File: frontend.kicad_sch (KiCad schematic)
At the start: 76 parts, among them J10 GND_CLIP, J3 RF-SHIELD-FRAME, J4 MOUNTING_HOLE, J5 MOUNTING_HOLE, J6 MOUNTING_HOLE, J7 MOUNTING_HOLE, P4 SMA, Q1 NMOS/PMOS, Q14 Q_PMOS_GSD, Q8 BFR840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

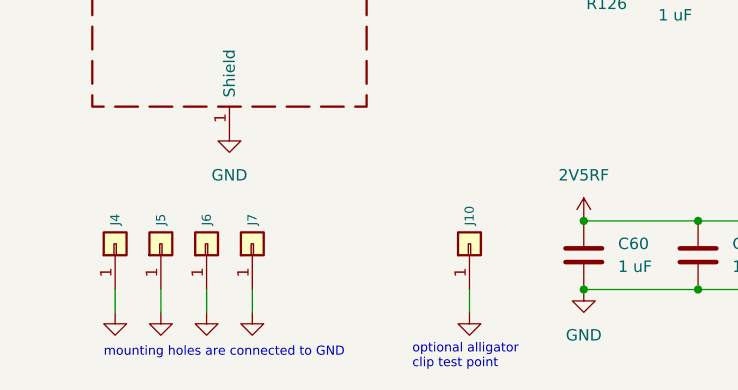
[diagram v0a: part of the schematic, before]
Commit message: Update symbols and footprints
- Update U21 symbol and footprint
- Add L10, L11 3D model
- Add T1, T2 3D model
- Update U29 footprint
- Update J10 footprint and part selection, change to TP6
- Update diode footprints and 3D models
- Update SMA connector footprint
- Fix 3D model scale for various footprints
- Change L1 from 0603 back to 0201
- Fix pin header 3D models
- Add component substitutions
- Update RF switch and amplifier footprints
- Remove fiducials
- Update mounting hole symbol and footprint
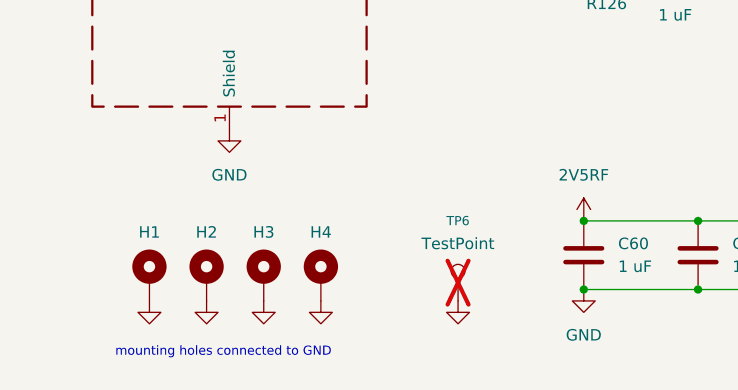
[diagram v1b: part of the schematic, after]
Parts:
- removed J4, J5, J6, J7: MOUNTING_HOLE, hackrf:GSG-HOLE126MIL-COPPER, symbol Connector_Generic:Conn_01x01
- added H1, H2, H3, H4: MountingHole_Pad, praline:MountingHole_3.2mm_M3_Pad_Via, symbol Mechanical:MountingHole_Pad
- P4: Substitution (none) -> M04-0102170R0A
- TP6: renamed from J10; value GND_CLIP -> TestPoint; footprint hackrf:GSG-TEST-POINT-S1751-46R -> TestPoint:TestPoint_Loop_D1.80mm_Drill1.0mm_Beaded; symbol Connector_Generic:Conn_01x01 -> Connector:TestPoint; Manufacturer Harwin -> Ronghe; Part Number S1751-46R -> RH-5001; now not fitted
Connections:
- net GND: now also H1.1, H2.1, H3.1, H4.1
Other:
- note added: "mounting holes connected to GND"
- note removed: "mounting holes are connected to GND"
- note removed: "optional alligator clip test point"

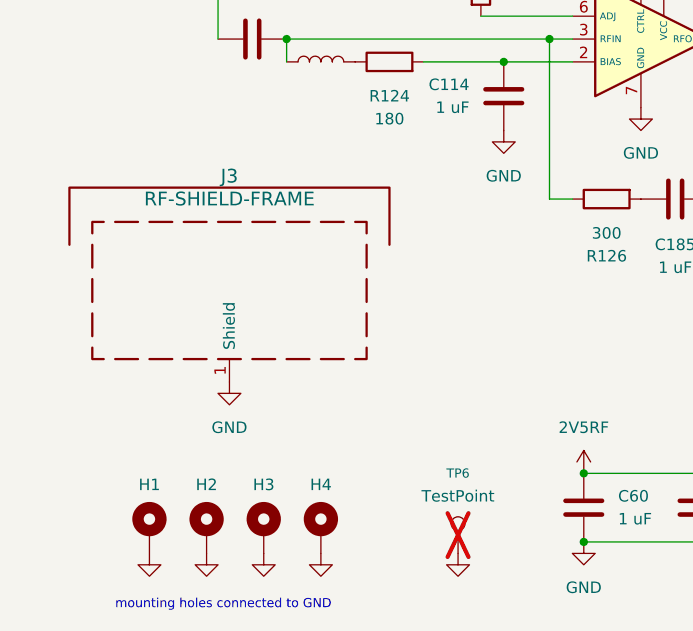
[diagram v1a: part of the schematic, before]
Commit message: Add M2 mounting holes
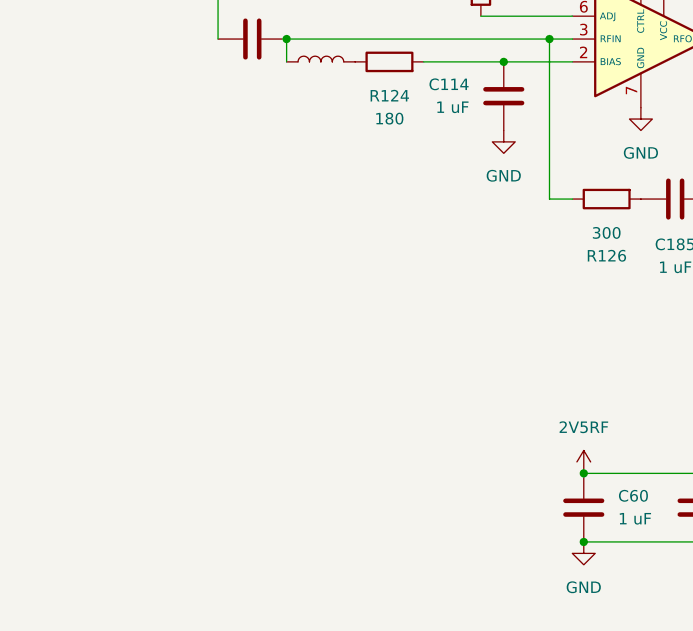
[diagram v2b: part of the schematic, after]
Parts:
- removed H1, H2, H3, H4: MountingHole_Pad, praline:MountingHole_3.2mm_M3_Pad_Via, symbol Mechanical:MountingHole_Pad
- removed J3: RF-SHIELD-FRAME, praline:Laird_Technologies_BMI-S-230-F_50.8x38.1mm, symbol Device:RFShield_TwoPieces
- removed TP6: TestPoint, TestPoint:TestPoint_Loop_D1.80mm_Drill1.0mm_Beaded, symbol Connector:TestPoint
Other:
- note removed: "mounting holes connected to GND"

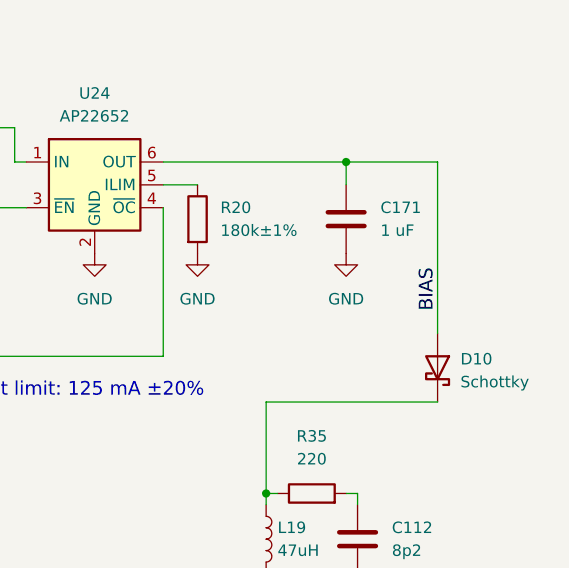
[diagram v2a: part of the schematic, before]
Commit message: Add test points
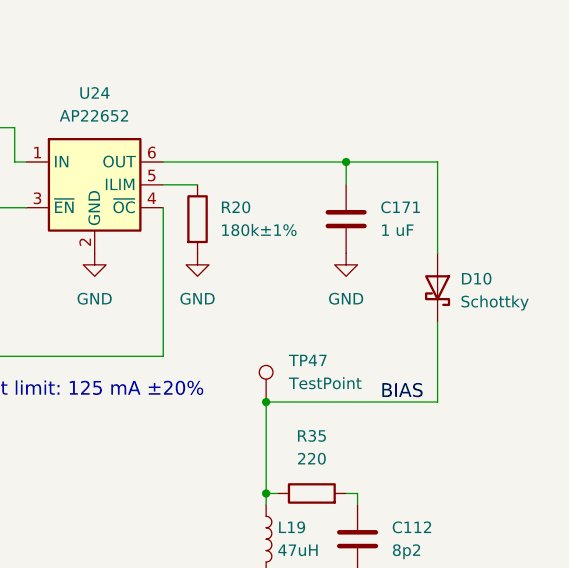
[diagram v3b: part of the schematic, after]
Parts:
- added TP47: TestPoint, TestPoint:TestPoint_Pad_D1.0mm, symbol Connector:TestPoint
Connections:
- net BIAS: now also D10.1 (K), L19.1, R35.1, TP47.1; no longer C171.1, D10.2 (A), U24.6 (OUT)
- new net: C171.1, D10.2 (A), U24.6 (OUT)
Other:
- moved on the sheet: D10
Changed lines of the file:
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@@
 	)
 	(junction
+		(at 241.3 64.77)
+		(diameter 0)
+		(color 0 0 0 0)
+	)
+	(junction
 		(at 143.51 63.5)
 		(diameter 0)
@@
 	(wire
 		(pts
+			(xy 241.3 64.77) (xy 260.35 64.77)
+		)
+		(stroke
+			(width 0)
+			(type default)
+		)
+	)
+	(wire
+		(pts
 			(xy 143.51 38.1) (xy 143.51 45.72)
 		)
@@
 	(wire
 		(pts
+			(xy 260.35 55.88) (xy 260.35 64.77)
+		)
+		(stroke
+			(width 0)
+			(type default)
+		)
+	)
+	(wire
+		(pts
 			(xy 191.77 132.08) (xy 193.04 132.08)
 		)
@@
 	(wire
 		(pts
-			(xy 260.35 57.15) (xy 260.35 38.1)
+			(xy 260.35 48.26) (xy 260.35 38.1)
 		)
 		(stroke
@@
 	(wire
 		(pts
-			(xy 260.35 64.77) (xy 241.3 64.77)
-		)
-		(stroke
-			(width 0)
-			(type default)
-		)
-	)
-	(wire
-		(pts
 			(xy 143.51 53.34) (xy 171.45 53.34)
 		)
@@
 	)
 	(label "BIAS"
-		(at 260.35 54.61 90)
+		(at 254 64.77 0)
 		(effects
 			(font
@@
 	(symbol
 		(lib_id "Device:D_Schottky")
-		(at 260.35 60.96 270)
+		(at 260.35 52.07 270)
 		(mirror x)
 		(unit 1)
@@
 		(fields_autoplaced yes)
 		(property "Reference" "D10"
-			(at 262.89 60.0074 90)
+			(at 262.89 51.1174 90)
 			(effects
 				(font
@@
 		)
 		(property "Value" "Schottky"
-			(at 262.89 62.5474 90)
+			(at 262.89 53.6574 90)
 			(effects
 				(font
@@
 		)
 		(property "Footprint" "praline:TSLP-2-19"
-			(at 260.35 60.96 0)
+			(at 260.35 52.07 0)
 			(effects
 				(font
@@
 		)
 		(property "Datasheet" "~"
-			(at 260.35 60.96 0)
+			(at 260.35 52.07 0)
 			(effects
 				(font
@@
 		)
 		(property "Description" "DIODE SCHOTTKY 40V 1A DSN1006-2"
-			(at 260.35 60.96 0)
+			(at 260.35 52.07 0)
 			(effects
 				(font
@@
 		)
 		(property "Manufacturer" "Nexperia"
-			(at 260.35 60.96 0)
+			(at 260.35 52.07 0)
 			(effects
 				(font
@@
 		)
 		(property "Part Number" "PMEG4010ESBYL"
-			(at 260.35 60.96 0)
+			(at 260.35 52.07 0)
 			(effects
 				(font
@@
 					(unit 1)
 				)
+			)
+		)
+	)
+	(symbol
+		(lib_id "Connector:TestPoint")
+		(at 241.3 64.77 0)
+		(unit 1)
+		(exclude_from_sim no)
+		(in_bom no)
+		(on_board yes)
+		(dnp no)
+		(fields_autoplaced yes)
+		(property "Reference" "TP47"
+			(at 243.84 60.1979 0)
+			(effects
+				(font
+					(size 1.27 1.27)
+				)
+				(justify left)
+			)
+		)
+		(property "Value" "TestPoint"
+			(at 243.84 62.7379 0)
+			(effects
+				(font
+					(size 1.27 1.27)
+				)
+				(justify left)
+			)
+		)
+		(property "Footprint" "TestPoint:TestPoint_Pad_D1.0mm"
+			(at 246.38 64.77 0)
+			(effects
+				(font
+					(size 1.27 1.27)
+				)
+				(hide yes)
+			)
+		)
+		(property "Datasheet" "~"
+			(at 246.38 64.77 0)
+			(effects
+				(font
+					(size 1.27 1.27)
+				)
+				(hide yes)
+			)
+		)
+		(property "Description" ""
+			(at 241.3 64.77 0)
+			(effects
+				(font
+					(size 1.27 1.27)
+				)
+				(hide yes)
+			)
+		)
+		(pin "1"
+		)
+		(instances
+			(project "praline"
+				(path "/dba4afc6-760f-46cb-a936-032b76448f03/00000000-0000-0000-0000-0000503bb638"
+					(reference "TP47")
+					(unit 1)
+				)

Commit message: Use consistent footprints for 0402 and 0201 diodes
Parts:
- D1: footprint Diode_SMD:Nexperia_DSN0603-2_0.6x0.3mm_P0.4mm -> praline:TSSLP-2-1
- Q14: Manufacturer NRC -> LRC
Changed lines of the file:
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@@
 			)
 		)
-		(property "Manufacturer" "NRC"
+		(property "Manufacturer" "LRC"
 			(at 148.59 33.02 0)
 			(effects
@@
 			)
 		)
-		(property "Footprint" "Diode_SMD:Nexperia_DSN0603-2_0.6x0.3mm_P0.4mm"
+		(property "Footprint" "praline:TSSLP-2-1"
 			(at 246.38 105.41 0)
 			(effects

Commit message: Correct component metadata
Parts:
- R43: Part Number RC0402JR-073RL -> RC0201JR-073RL
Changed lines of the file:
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@@
 			)
 		)
-		(property "Description" "RES 3 OHM 5% 1/16W 0402"
+		(property "Description" "RES 3 OHM 5% 1/20W 0201"
 			(at 113.03 129.54 0)
 			(effects
@@
 			)
 		)
-		(property "Part Number" "RC0402JR-073RL"
+		(property "Part Number" "RC0201JR-073RL"
 			(at 113.03 129.54 90)
 			(effects
@@
 					(size 1.27 1.27)
 				)
-				(hide yes)
 			)
 		)
@@
 					(size 1.27 1.27)
 				)
-				(hide yes)
-			)
-		)
+			)
+		)

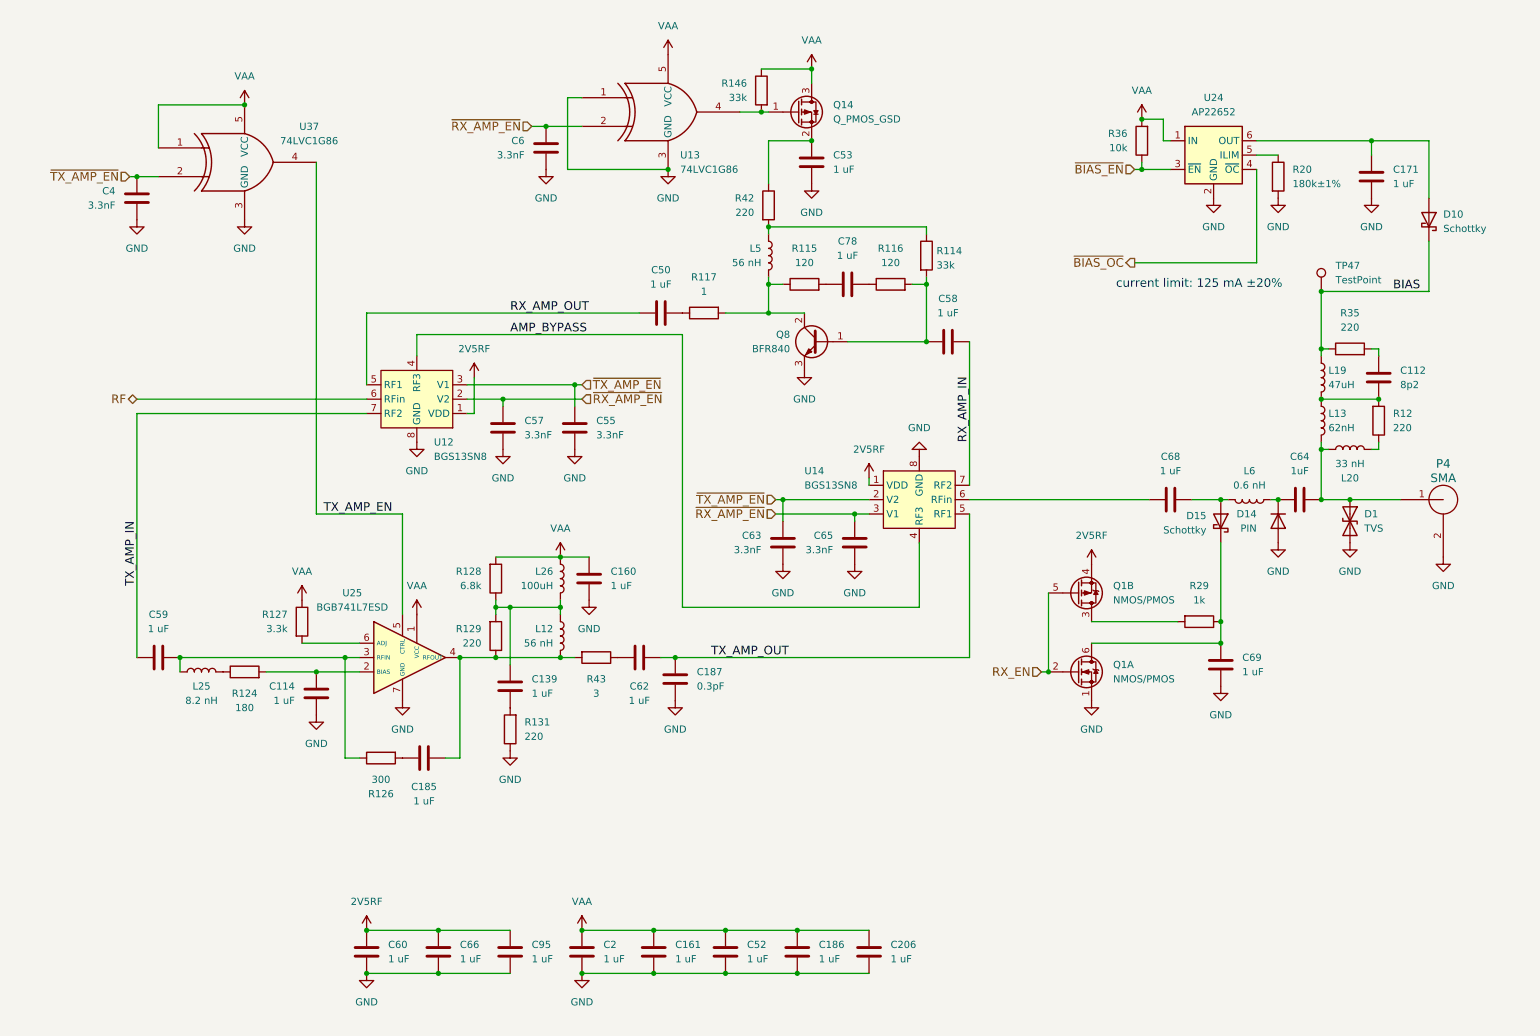
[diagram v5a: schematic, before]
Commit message: Change RX RF amplifier to BGB741
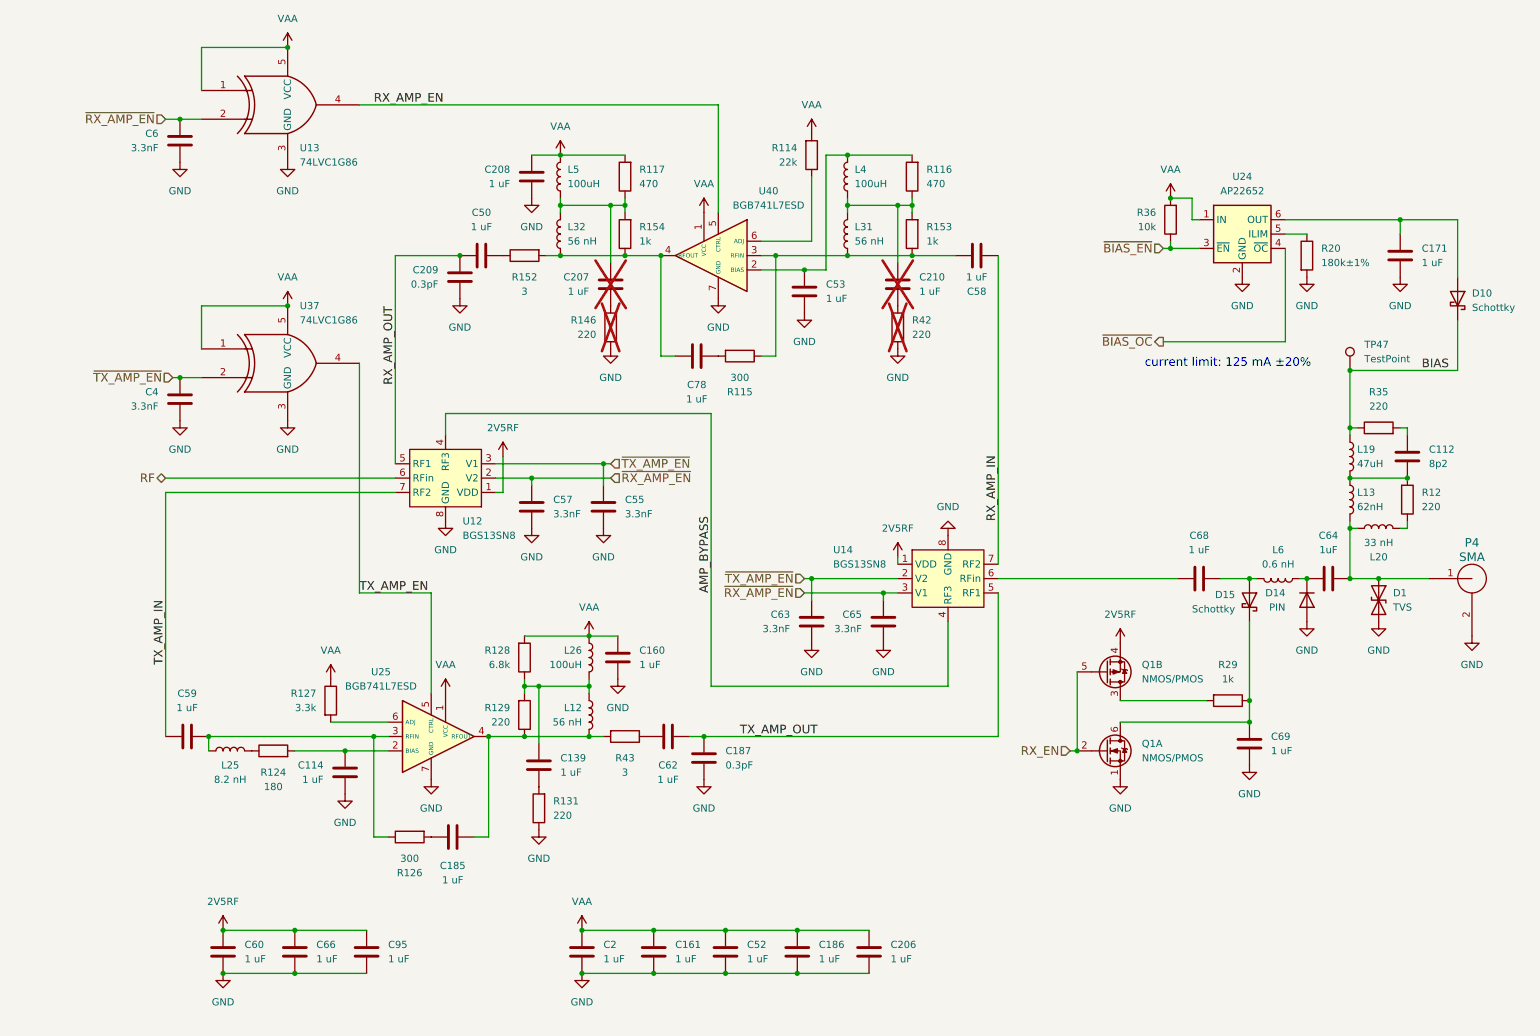
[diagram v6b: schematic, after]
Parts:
- removed Q14: Q_PMOS_GSD, praline:TSLP-3-9, symbol Transistor_FET:Q_PMOS_GSD
- removed Q8: BFR840, praline:TSLP-3-9, symbol Transistor_BJT:Q_NPN_BCE
- added C207, C208, C210: 1 uF, Capacitor_SMD:C_0201_0603Metric, symbol Device:C
- added C209: 0.3pF, Capacitor_SMD:C_0201_0603Metric, symbol Device:C
- added L31, L32: 56 nH, Inductor_SMD:L_0201_0603Metric, symbol Device:L
- added L4: 100uH, praline:L_TDK_MLZ2012_h1.25mm, symbol Device:L
- added R152: 3, Resistor_SMD:R_0201_0603Metric, symbol Device:R
- added R153, R154: 1k, Resistor_SMD:R_0201_0603Metric, symbol Device:R
- added U40: BGB741L7ESD, praline:TSLP-7-1, symbol praline:BGB741L7ESD
- L5: value 56 nH -> 100uH; footprint Inductor_SMD:L_0201_0603Metric -> praline:L_TDK_MLZ2012_h1.25mm; Manufacturer Murata -> TDK; Part Number LQP03TN56NJ02D -> MLZ2012N101LT000; Substitution LQP03TN56NH02D -> MLZ2012N101LTD25
- R114: value 33k -> 22k; Part Number RC0201JR-0733KL -> RC0201FR-0722K6L
- R115: value 120 -> 300; Part Number RC0201FR-07120RL -> RC0201FR-07300RL
- R116: value 120 -> 470; Part Number RC0201FR-07120RL -> RC0201JR-07470RL
- R117: value 1 -> 470; Part Number RC0201JR-071RL -> RC0201JR-07470RL
- R146: value 33k -> 220; Part Number RC0201JR-0733KL -> RC0201JR-07220RL; now not fitted
- R42: now not fitted
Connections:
- net GND: now also R146.1, R42.1, C208.2, C209.2, U40.7 (GND); no longer U13.1
- net RX_AMP_OUT: now also C209.1
- net VAA: now also L5.1, R114.2, R117.2, U13.1, C208.1, U40.1 (VCC); no longer R146.1
- net at C53.1: now also R116.2, L4.1, U40.2 (BIAS); no longer R42.1
- net at C50.2: now also R152.1; no longer R117.1
- net at R146.2: now also C207.2; no longer U13.4
- net at C78.1: now also L32.2, R152.2, R154.1, U40.4 (RFOUT); no longer R115.2
- net at R116.1: now also C210.1, L31.1, L4.2, R153.2; no longer C78.2
- new net: C58.2, L31.2, R115.1, R153.1, U40.3 (RFIN)
- new net: C78.2, R115.2
- new net: R114.1, U40.6 (ADJ)
- new net: C207.1, L32.1, L5.2, R117.1, R154.2
- new net: C210.2, R42.2
- new net RX_AMP_EN: U13.4, U40.5 (CTRL)
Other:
- moved on the sheet: C112, C114, C139, C160, C171, C185, C187, C4, C50, C55, C57, C58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
